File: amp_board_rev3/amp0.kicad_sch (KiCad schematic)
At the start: 29 parts, among them U3 PA343, U4 SMCJ150A, U7 SMCJ150A, U8 PA343, U9 PA343

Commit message: routing complete
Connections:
- net GND: now also U9.25 (EPAD), U9.26, U9.27
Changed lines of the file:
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@@
 	)
 	(junction
+		(at 182.88 97.79)
+		(diameter 0)
+		(color 0 0 0 0)
+	)
+	(junction
 		(at 163.83 34.29)
 		(diameter 0)
@@
 	(wire
 		(pts
+			(xy 182.88 100.33) (xy 182.88 97.79)
+		)
+		(stroke
+			(width 0)
+			(type default)
+		)
+	)
+	(wire
+		(pts
 			(xy 44.45 38.1) (xy 166.37 38.1)
 		)
@@
 	(wire
 		(pts
+			(xy 182.88 97.79) (xy 182.88 95.25)
+		)
+		(stroke
+			(width 0)
+			(type default)
+		)
+	)
+	(wire
+		(pts
 			(xy 44.45 43.18) (xy 44.45 38.1)
 		)
@@
 	(wire
 		(pts
+			(xy 185.42 97.79) (xy 182.88 97.79)
+		)
+		(stroke
+			(width 0)
+			(type default)
+		)
+	)
+	(wire
+		(pts
 			(xy 168.91 140.97) (xy 168.91 143.51)
 		)
@@
 	(wire
 		(pts
+			(xy 185.42 93.98) (xy 185.42 97.79)
+		)
+		(stroke
+			(width 0)
+			(type default)
+		)
+	)
+	(wire
+		(pts
 			(xy 242.57 44.45) (xy 281.94 44.45)
 		)
@@
 	(symbol
 		(lib_id "power:GND")
-		(at 182.88 95.25 0)
+		(at 182.88 100.33 0)
 		(unit 1)
 		(exclude_from_sim no)
@@
 		(fields_autoplaced yes)
 		(property "Reference" "#PWR033"
-			(at 182.88 101.6 0)
+			(at 182.88 106.68 0)
 			(effects
 				(font
@@
 		)
 		(property "Value" "GND"
-			(at 182.88 100.33 0)
+			(at 182.88 105.41 0)
 			(effects
 				(font
@@
 		)
 		(property "Footprint" ""
-			(at 182.88 95.25 0)
+			(at 182.88 100.33 0)
 			(effects
 				(font
@@
 		)
 		(property "Datasheet" ""
-			(at 182.88 95.25 0)
+			(at 182.88 100.33 0)
 			(effects
 				(font
@@
 		)
 		(property "Description" "Power symbol creates a global label with name \"GND\" , ground"
-			(at 182.88 95.25 0)
+			(at 182.88 100.33 0)
 			(effects
 				(font

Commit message: all routed
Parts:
- added R38, R40: 10, Resistor_SMD:R_0603_1608Metric, symbol Device:R_US
- added R39, R41: 100, Resistor_SMD:R_0603_1608Metric, symbol Device:R_US
- renumbered C3 to C15, C4 to C16, C5 to C17, C6 to C18, C11 to C23, C12 to C24, C13 to C25, R8 to R20, R9 to R21, R10 to R22, R11 to R23, R12 to R24, R13 to R25, U4 to U10, U3 to U9
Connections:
- net GND: now also R39.1, R41.1; no longer C21.2, C22.2 (-), C25.2, C26.2 (-), U10.2 (A), U7.2 (A), U8.12, U8.24, U8.25 (EPAD), U8.26, U8.27, U8.9 (+IN_B), U9.12, U9.24, U9.25 (EPAD), U9.26, U9.27, U9.9 (+IN_B)
- net input_0a_lv: now also R38.1, R39.2; no longer C15.2
- net input_1a_lv: now also R40.1, R41.2; no longer C16.2
- new net: C15.2, R38.2
- new net: C16.2, R40.2
- new net VSS: C21.2, C22.2 (-), C25.2, C26.2 (-), U10.2 (A), U7.2 (A), U8.12, U8.24, U8.25 (EPAD), U8.26, U8.27, U8.9 (+IN_B), U9.12, U9.24, U9.25 (EPAD), U9.26, U9.27, U9.9 (+IN_B)

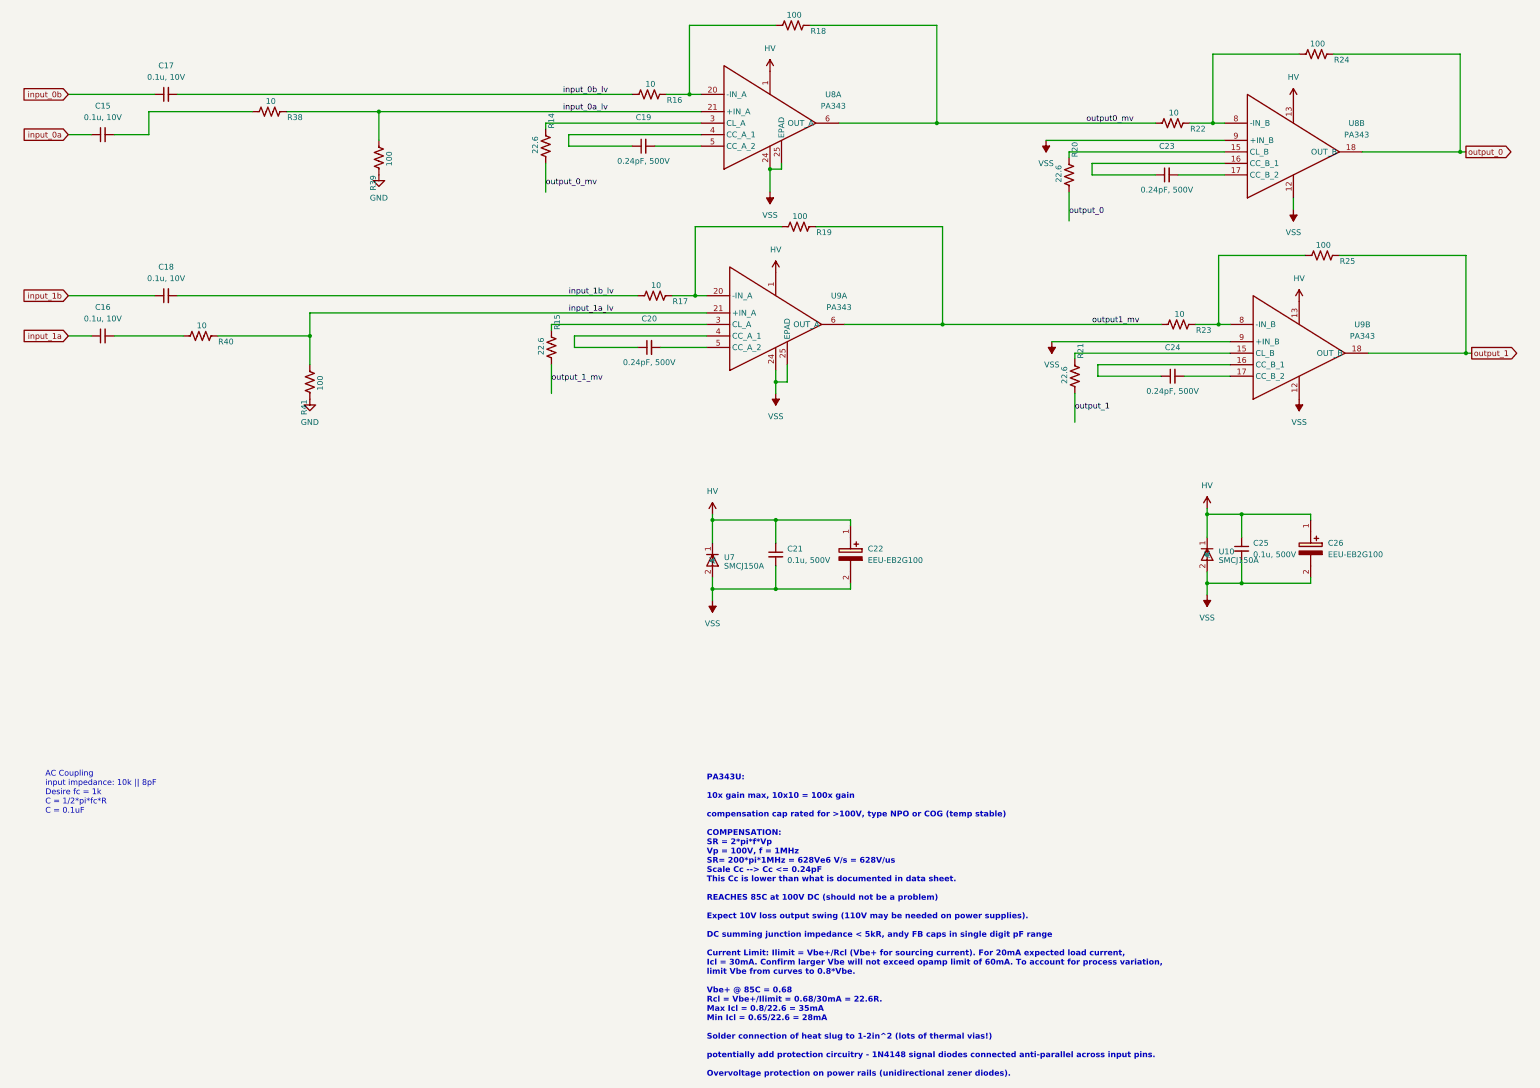
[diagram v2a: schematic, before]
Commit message: updated ground references in schematic
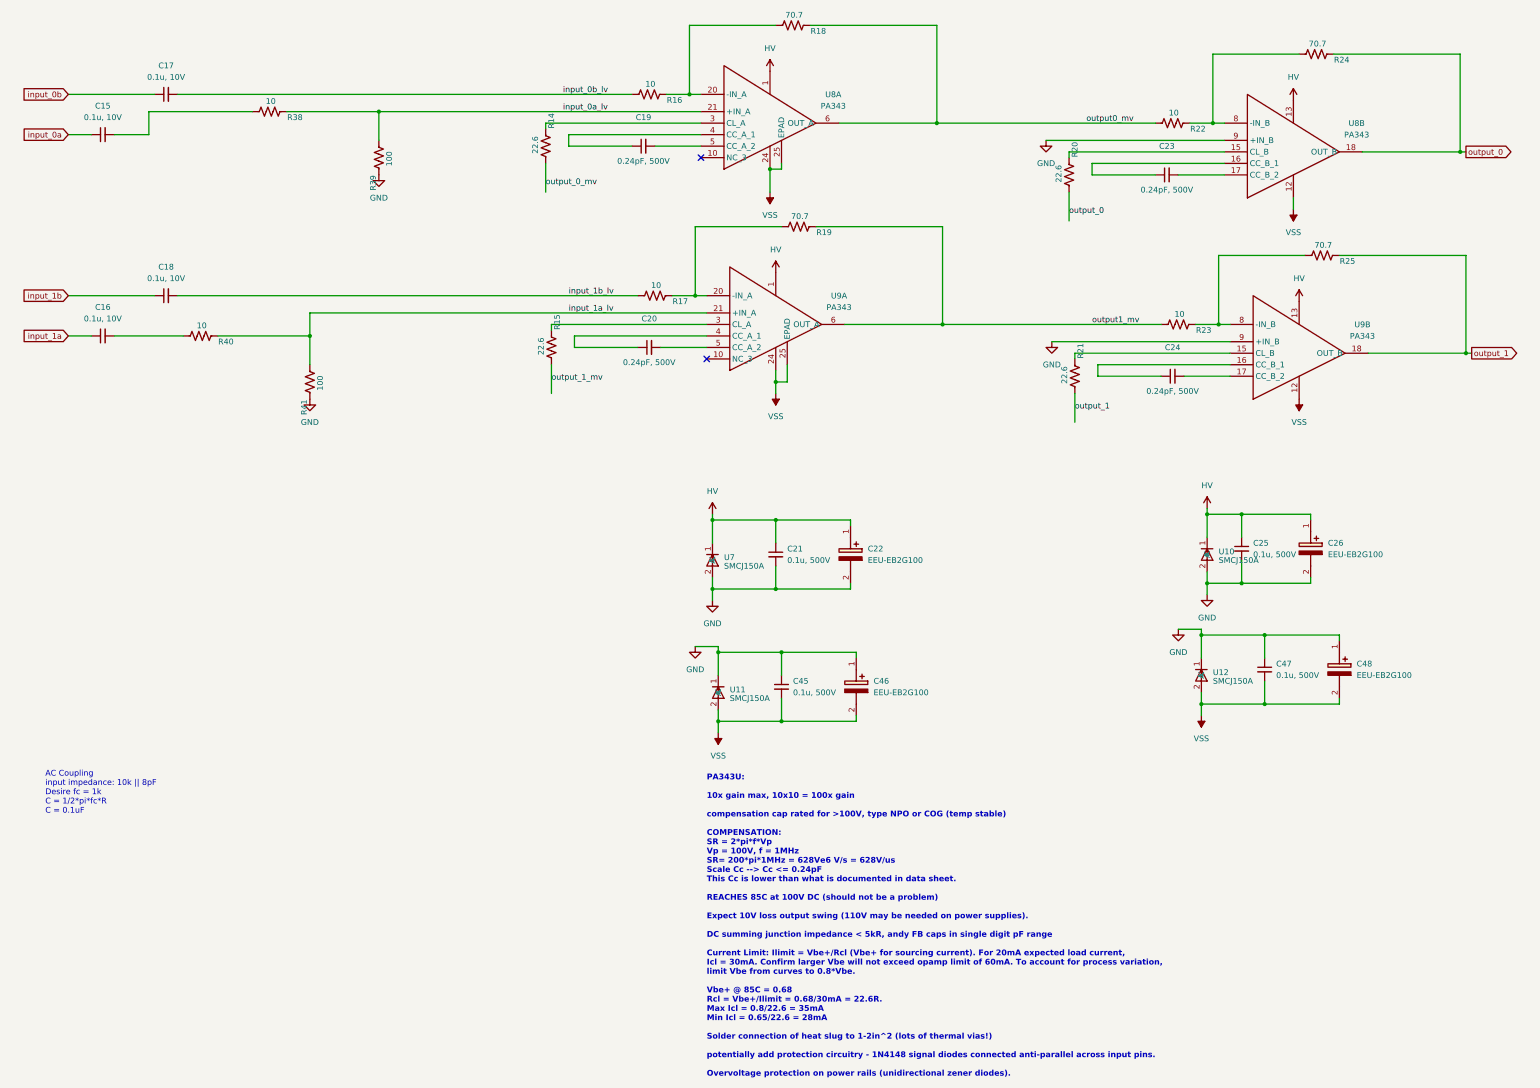
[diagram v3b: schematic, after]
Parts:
- added C45, C47: 0.1u, 500V, Capacitor_SMD:C_1812_4532Metric, symbol Device:C_Small
- added C46, C48: EEU-EB2G100, 726_footprints:EEU-EB2G100, symbol _PHASE:EEU-EB2G100
- added U11, U12: SMCJ150A, 726_footprints:SMCJ150A-13-F, symbol _PHASE:SMCJ150A-13-F
- R18, R19, R24, R25: value 100 -> 70.7
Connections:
- net GND: now also C21.2, C22.2 (-), C25.2, C26.2 (-), U10.2 (A), U7.2 (A), U8.9 (+IN_B), U9.9 (+IN_B), C45.1, C46.1 (+), C47.1, C48.1 (+), U11.1 (K), U12.1 (K)
- net VSS: now also C45.2, C46.2 (-), C47.2, C48.2 (-), U11.2 (A), U12.2 (A); no longer C21.2, C22.2 (-), C25.2, C26.2 (-), U10.2 (A), U7.2 (A), U8.9 (+IN_B), U9.9 (+IN_B)
- no-connect marks 0 -> 2

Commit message: updates based on 11/14 meeting
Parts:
- C15, C16, C17, C18: footprint Capacitor_SMD:C_0603_1608Metric -> (none)
- C19, C20: value 0.24pF, 500V -> 0.75pF, 250V; footprint Capacitor_SMD:C_0402_1005Metric -> (none)
- C21, C25, C45, C47: footprint Capacitor_SMD:C_1812_4532Metric -> (none)
- C22, C26, C46, C48: footprint 726_footprints:EEU-EB2G100 -> CAPPRD500W65D1000H2200
- C23, C24: value 0.24pF, 500V -> 0.2pF, 250V; footprint Capacitor_SMD:C_0402_1005Metric -> (none)
- R14, R15, R16, R17, R18, R19, R20, R21, R22, R23, R24, R25, R38, R39, R40, R41: footprint Resistor_SMD:R_0603_1608Metric -> (none)
- U8, U9: footprint 726_footprints:PA341DF -> (none)
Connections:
- now unconnected: U8.10 (NC_3), U8.11 (NC_4), U8.14 (NC_5), U8.7 (NC_2), U9.10 (NC_3), U9.11 (NC_4), U9.14 (NC_5), U9.7 (NC_2)

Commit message: detailed adjustments
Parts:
- removed unit 2 of U8
- removed unit 2 of U9
- added unit 2 of U8
- added unit 2 of U9
- C15, C16, C17, C18: footprint (none) -> Capacitor_SMD:C_0603_1608Metric
- C19, C20, C23, C24: footprint (none) -> Capacitor_SMD:C_0805_2012Metric
- C21, C25, C45, C47: footprint (none) -> Capacitor_SMD:C_1812_4532Metric
- C22, C26, C46, C48: footprint CAPPRD500W65D1000H2200 -> 726_footprints:EEU-EB2G100
- U8, U9: footprint (none) -> 726_footprints:PA341DF
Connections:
- net GND: now also U8.9 (+IN_B), U9.9 (+IN_B)
- net HV: now also U8.13, U9.13
- net VSS: now also U8.12, U9.12
- net output_0: now also U8.18 (OUT_B)
- net output_1: now also U9.18 (OUT_B)
- net at R21.1: now also U9.15 (CL_B)
- net at R20.1: now also U8.15 (CL_B)
- net at C23.1: now also U8.16 (CC_B_1)
- net at C23.2: now also U8.17 (CC_B_2)
- net at R23.1, R25.2: now also U9.8 (-IN_B)
- net at C24.1: now also U9.16 (CC_B_1)
- net at C24.2: now also U9.17 (CC_B_2)
- net at R22.1, R24.2: now also U8.8 (-IN_B)
- no-connect marks 2 -> 18

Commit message: final fabrication generated
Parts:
- R16, R17, R22, R23, R38, R40: value 10 -> 100
- R18, R19, R24, R25: value 70.7 -> 707
- R39, R41: value 100 -> 707
